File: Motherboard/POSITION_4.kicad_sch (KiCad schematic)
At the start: 27 parts, among them Q16 MOSFET_N_(ZVN3320FTA), Q18 MOSFET_N_(DMN61D8LQ-13)

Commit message: Schematic ready.  Going to clean up directory now.
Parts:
- C25, C35, C36, C37, C38: footprint Capacitors_SMD:C_1206 -> Capacitor_SMD:C_1206_3216Metric
- CAL7, CAL8: footprint (none) -> Smart_Tank:FEMALE_SPADE_QC_(TE_63969-1)
- CTRL_SHUNT_4, PUMP_SHUNT_4: footprint _GARRETTS_PARTS:SHUNT_(WSL40261L000FEA) -> Smart_Tank:SHUNT_(WSL40261L000FEA)
- D10, D5: footprint Diodes_SMD:SOD-123 -> Diode_SMD:D_SMA
- Q16: footprint TO_SOT_Packages_SMD:SOT-23 -> Package_TO_SOT_SMD:SOT-23
- R10, R67, R70, R73, R74, R75: footprint Resistors_SMD:R_1206 -> Resistor_SMD:R_1206_3216Metric
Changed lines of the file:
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@@
 			)
 		)
-		(property "Footprint" "_GARRETTS_PARTS:SHUNT_(WSL40261L000FEA)"
+		(property "Footprint" "Smart_Tank:SHUNT_(WSL40261L000FEA)"
 			(at 195.58 140.208 90)
 			(effects
@@
 			)
 		)
-		(property "Footprint" ""
+		(property "Footprint" "Smart_Tank:FEMALE_SPADE_QC_(TE_63969-1)"
 			(at 195.58 107.95 0)
 			(effects
@@
 			)
 		)
-		(property "Footprint" "_GARRETTS_PARTS:SHUNT_(WSL40261L000FEA)"
+		(property "Footprint" "Smart_Tank:SHUNT_(WSL40261L000FEA)"
 			(at 195.58 53.848 90)
 			(effects
@@
 			)
 		)
-		(property "Footprint" "Diodes_SMD:SOD-123"
+		(property "Footprint" "Diode_SMD:D_SMA"
 			(at 254 41.91 0)
 			(effects
@@
 			)
 		)
-		(property "Footprint" "Resistors_SMD:R_1206"
+		(property "Footprint" "Resistor_SMD:R_1206_3216Metric"
 			(at 74.168 43.18 90)
 			(effects
@@
 			)
 		)
-		(property "Footprint" "Resistors_SMD:R_1206"
+		(property "Footprint" "Resistor_SMD:R_1206_3216Metric"
 			(at 117.348 81.28 90)
 			(effects
@@
 			)
 		)
-		(property "Footprint" "Capacitors_SMD:C_1206"
+		(property "Footprint" "Capacitor_SMD:C_1206_3216Metric"
 			(at 219.4052 53.34 0)
 			(effects
@@
 			)
 		)
-		(property "Footprint" "Resistors_SMD:R_1206"
+		(property "Footprint" "Resistor_SMD:R_1206_3216Metric"
 			(at 101.6 92.202 90)
 			(effects
@@
 			)
 		)
-		(property "Footprint" "Capacitors_SMD:C_1206"
+		(property "Footprint" "Capacitor_SMD:C_1206_3216Metric"
 			(at 257.81 48.5648 0)
 			(effects
@@
 			)
 		)
-		(property "Footprint" "Capacitors_SMD:C_1206"
+		(property "Footprint" "Capacitor_SMD:C_1206_3216Metric"
 			(at 229.5652 139.7 0)
 			(effects
@@
 			)
 		)
-		(property "Footprint" "Capacitors_SMD:C_1206"
+		(property "Footprint" "Capacitor_SMD:C_1206_3216Metric"
 			(at 229.5652 53.34 0)
 			(effects
@@
 			)
 		)
-		(property "Footprint" "Capacitors_SMD:C_1206"
+		(property "Footprint" "Capacitor_SMD:C_1206_3216Metric"
 			(at 219.4052 139.7 0)
 			(effects
@@
 			)
 		)
-		(property "Footprint" "Resistors_SMD:R_1206"
+		(property "Footprint" "Resistor_SMD:R_1206_3216Metric"
 			(at 190.5 78.232 90)
 			(effects
@@
 			)
 		)
-		(property "Footprint" "Diodes_SMD:SOD-123"
+		(property "Footprint" "Diode_SMD:D_SMA"
 			(at 237.49 80.01 0)
 			(effects
@@
 			)
 		)
-		(property "Footprint" "Resistors_SMD:R_1206"
+		(property "Footprint" "Resistor_SMD:R_1206_3216Metric"
 			(at 94.488 99.06 90)
 			(effects
@@
 			)
 		)
-		(property "Footprint" "TO_SOT_Packages_SMD:SOT-23"
+		(property "Footprint" "Package_TO_SOT_SMD:SOT-23"
 			(at 119.38 94.615 0)
 			(effects
@@
 			)
 		)
-		(property "Footprint" ""
+		(property "Footprint" "Smart_Tank:FEMALE_SPADE_QC_(TE_63969-1)"
 			(at 254 33.02 0)
 			(effects
@@
 			)
 		)
-		(property "Footprint" "Resistors_SMD:R_1206"
+		(property "Footprint" "Resistor_SMD:R_1206_3216Metric"
 			(at 185.928 86.36 90)
 			(effects

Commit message: Started cleaning out old parts from PCB.
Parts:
- PUMP_V_CONN_4: footprint Smart_Tank:PHNX_TB_SCREW_4_POS_(1729144) -> Smart_Tank:PHX_TB_HDR_4_POS_STR_(1755752)
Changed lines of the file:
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@@
 			)
 		)
-		(property "Footprint" "Smart_Tank:PHNX_TB_SCREW_4_POS_(1729144)"
+		(property "Footprint" "Smart_Tank:PHX_TB_HDR_4_POS_STR_(1755752)"
 			(at 250.19 83.82 0)
 			(effects

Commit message: Almost done with re-routing.
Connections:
- net POS_4_SPARE renamed POS_4_SPR_1
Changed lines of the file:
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@@
 		)
 	)
-	(global_label "POS_4_SPARE"
+	(global_label "POS_4_SPR_1"
 		(shape input)
 		(at 58.42 59.69 0)

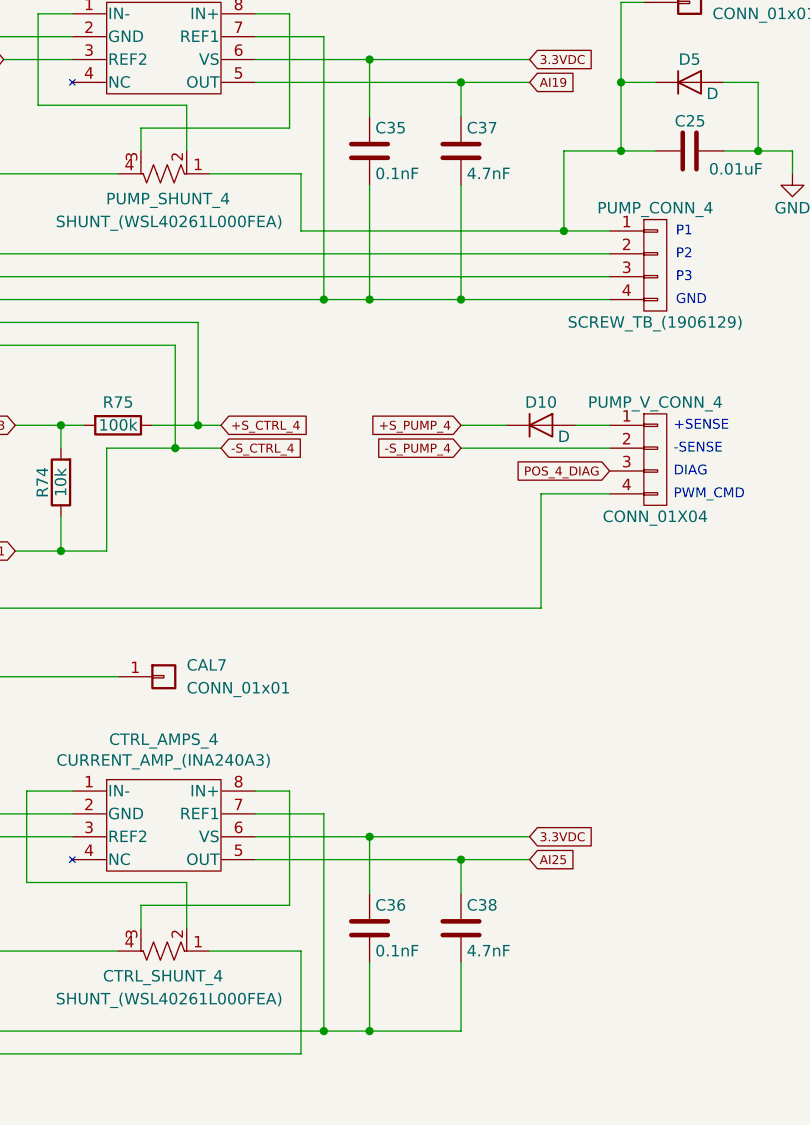
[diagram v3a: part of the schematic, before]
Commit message: Capacitor part issues...
Made these changes...

Concerning C13, C15, C27, C28, C31, C32, C35, C36, C39, C40, C43, C44
The schematic is wrong, and the BOM is correct.  These should all be 0.1uF
Concerning C20, C21, C29, C30, C33, C34, C37, C38, C41, C42, C45, C46
The BOM is wrong, and the schematic is correct.  These should all be 4.7nF
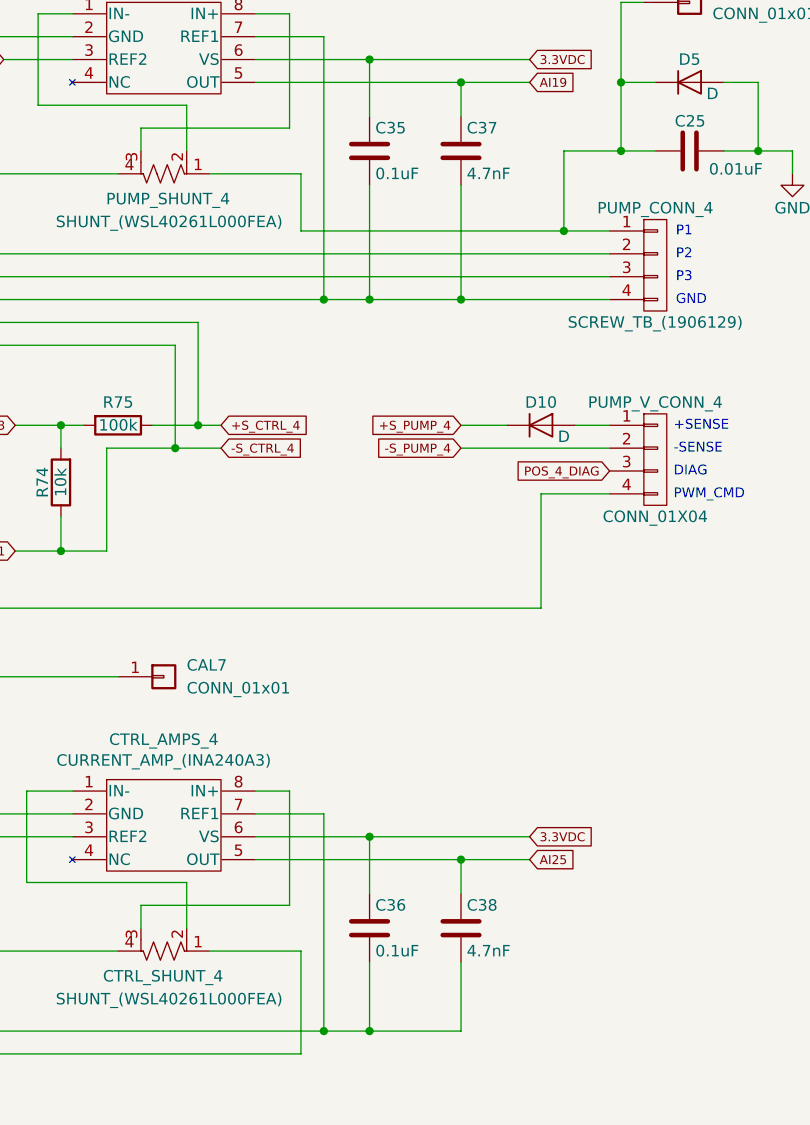
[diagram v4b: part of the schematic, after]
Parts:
- C35, C36: value 0.1nF -> 0.1uF
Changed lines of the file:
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@@
 			)
 		)
-		(property "Value" "0.1nF"
+		(property "Value" "0.1uF"
 			(at 219.075 52.07 0)
 			(effects
@@
 			)
 		)
-		(property "Value" "0.1nF"
+		(property "Value" "0.1uF"
 			(at 219.075 138.43 0)
 			(effects
